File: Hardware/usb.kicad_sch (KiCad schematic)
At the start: 8 parts, among them J2 USB_C_Receptacle_USB2.0

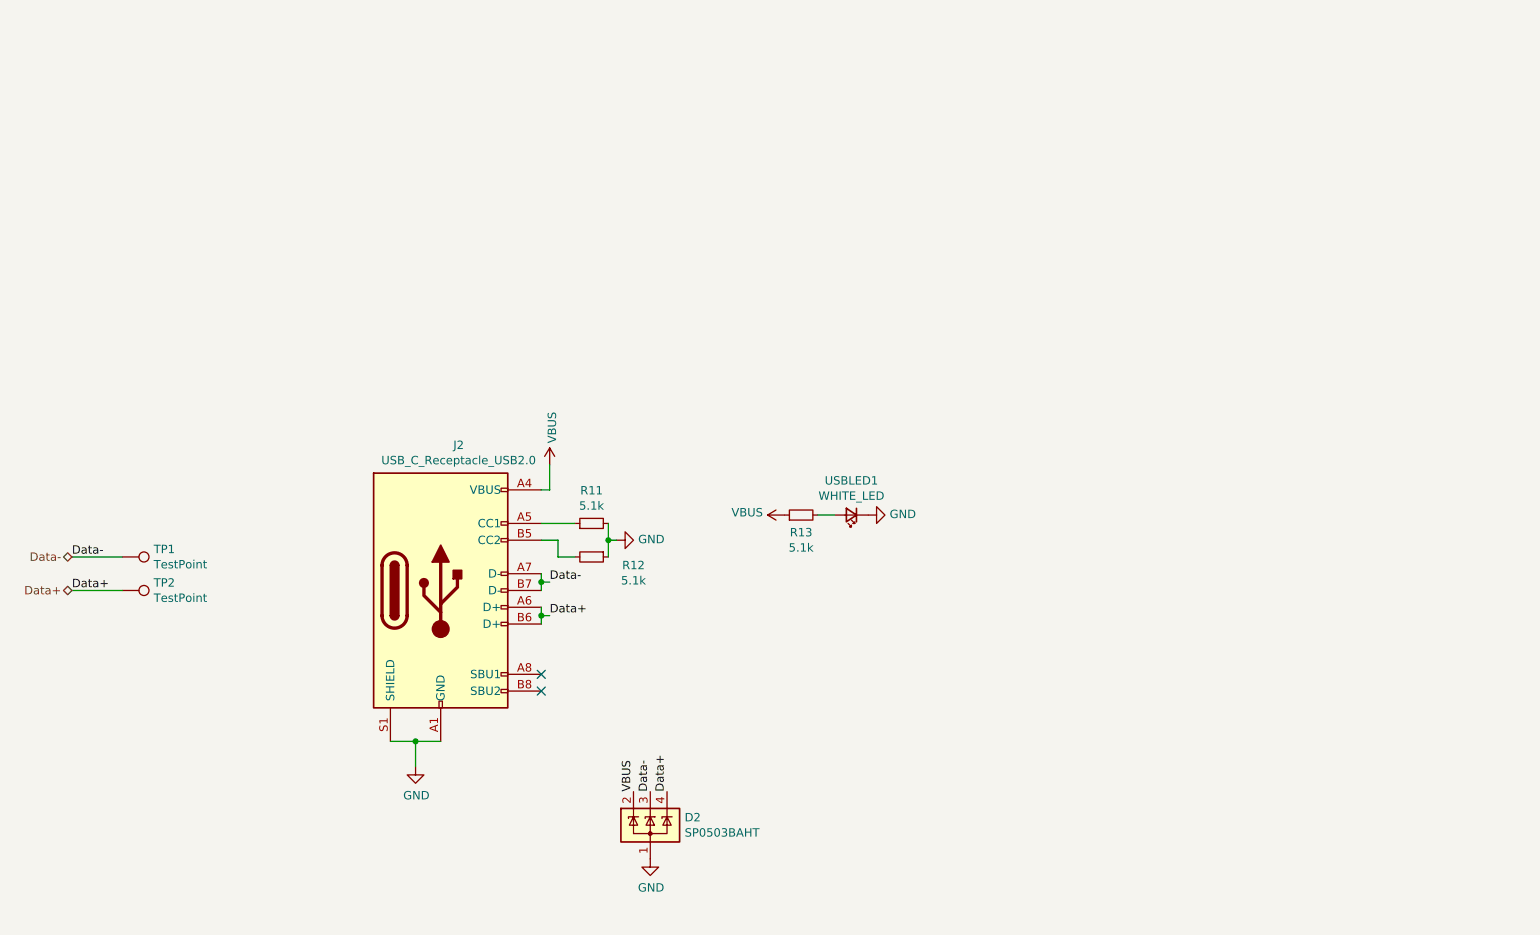
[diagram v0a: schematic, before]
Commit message: Revert "Merge remote-tracking branch 'refs/remotes/origin/main'"
This reverts commit c9a99cb72454eddb78504ad976151236a8d13e5c, reversing
changes made to 3cdb2e540a9938f01cf78ecb1078cc5742e66bb5.
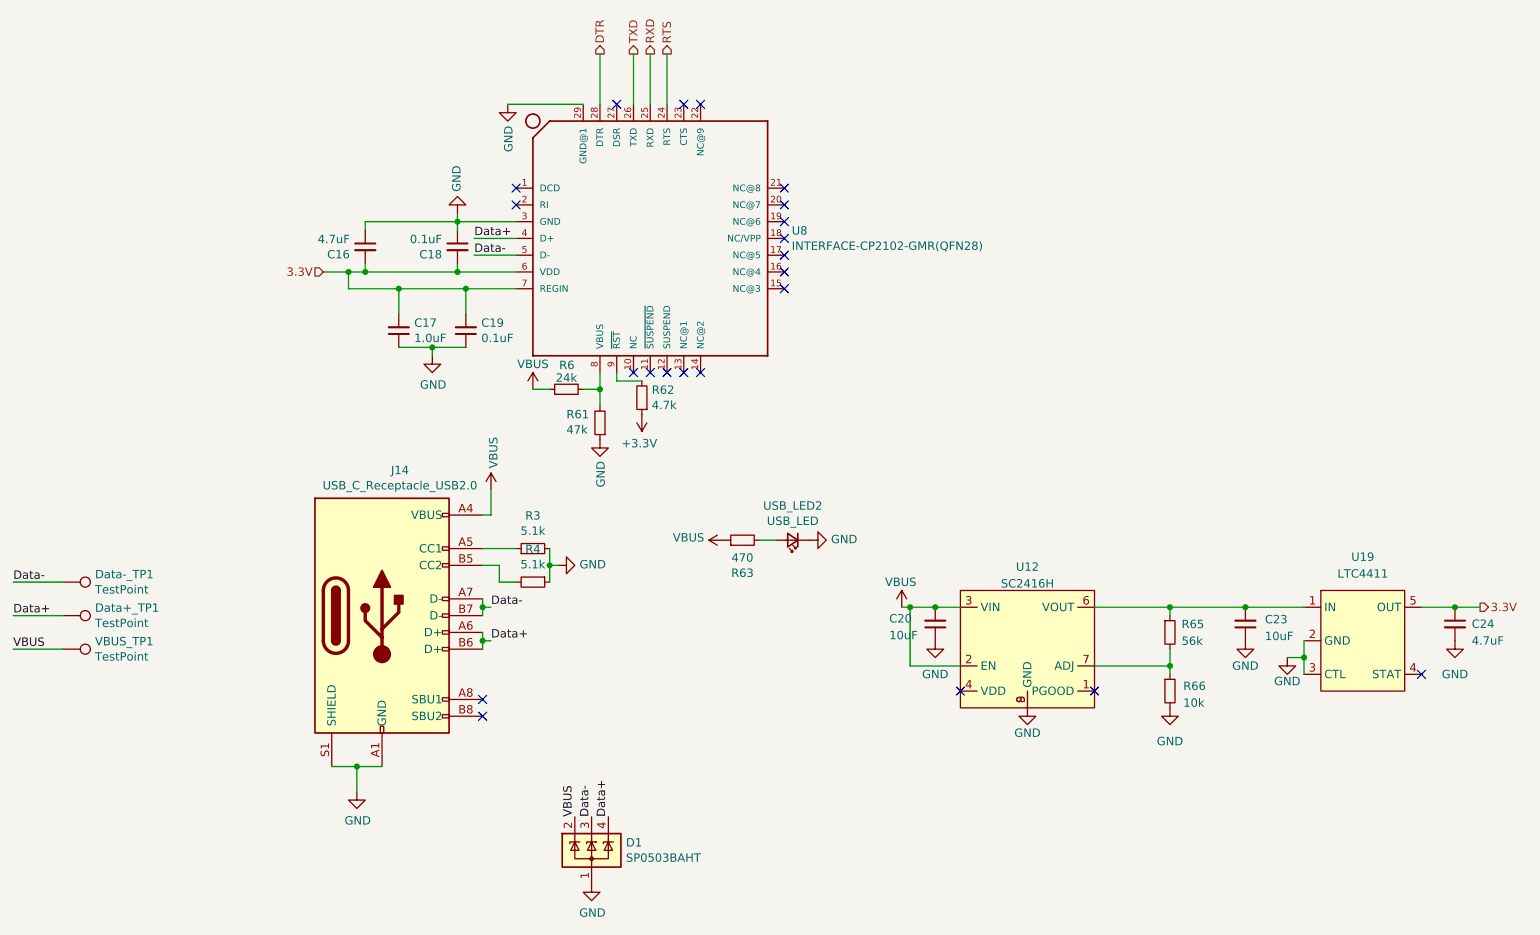
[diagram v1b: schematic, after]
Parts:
- removed D2: SP0503BAHT, Package_TO_SOT_SMD:SOT-143, symbol Power_Protection:SP0503BAHT
- removed J2: USB_C_Receptacle_USB2.0, Connector_USB:USB_C_Receptacle_Palconn_UTC16-G, symbol Connector:USB_C_Receptacle_USB2.0
- removed R11, R12, R13: 5.1k, Resistor_SMD:R_0402_1005Metric, symbol Device:R_Small
- removed TP1, TP2: TestPoint, TestPoint:TestPoint_Pad_D1.0mm, symbol Connector:TestPoint
- removed USBLED1: WHITE_LED, Resistor_SMD:R_0402_1005Metric, symbol Device:LED_Small
- added C16, C24: 4.7uF, Capacitor_SMD:C_0603_1608Metric, symbol Device:C_Small
- added C17: 1.0uF, Capacitor_SMD:C_0603_1608Metric, symbol Device:C_Small
- added C18, C19: 0.1uF, Capacitor_SMD:C_0603_1608Metric, symbol Device:C_Small
- added C20, C23: 10uF, Capacitor_SMD:C_0603_1608Metric, symbol Device:C_Small
- added D1: SP0503BAHT, Package_TO_SOT_SMD:SOT-143, symbol Power_Protection:SP0503BAHT
- added Data+_TP1, Data-_TP1, VBUS_TP1: TestPoint, TestPoint:TestPoint_Pad_D1.0mm, symbol Connector:TestPoint
- added J14: USB_C_Receptacle_USB2.0, Connector_USB:USB_C_Receptacle_GCT_USB4085, symbol Connector:USB_C_Receptacle_USB2.0
- added R3, R4: 5.1k, Resistor_SMD:R_0603_1608Metric, symbol Device:R_Small
- added R6: 24k, Resistor_SMD:R_0603_1608Metric, symbol Device:R_Small
- added R61: 47k, Resistor_SMD:R_0603_1608Metric, symbol Device:R_Small
- added R62: 4.7k, Resistor_SMD:R_0603_1608Metric, symbol Device:R_Small
- added R63: 470, Resistor_SMD:R_0603_1608Metric, symbol Device:R_Small
- added R65: 56k, Resistor_SMD:R_0603_1608Metric, symbol Device:R_Small
- added R66: 10k, Resistor_SMD:R_0603_1608Metric, symbol Device:R_Small
- added U12: SC2416H, iclr:SOIC127P599X175-9N, symbol iclr:RT9025-25GSP
- added U19: LTC4411, Package_TO_SOT_SMD:SOT-23-5, symbol iclr:LTC4411
- added U8: INTERFACE-CP2102-GMR(QFN28), iclr:QFN28G_0.5-5X5MM, symbol iclr:INTERFACE-CP2102-GMR(QFN28)
- added USB_LED2: USB_LED, LED_SMD:LED_0603_1608Metric, symbol Device:LED_Small
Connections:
- net Data+: now also D1.4 (K), Data+_TP1.1, J14.A6 (D+), J14.B6 (D+), U8.4 (D+)
- net Data-: now also D1.3 (K), Data-_TP1.1, J14.A7 (D-), J14.B7 (D-), U8.5 (D-)
- net GND: now also C16.1, C17.1, C18.1, C19.1, C20.1, C23.1, C24.2, D1.1 (A), J14.A1 (GND), J14.A12 (GND), J14.B1 (GND), J14.B12 (GND), J14.S1 (SHIELD), R3.2, R4.1, R61.1, R66.2, U12.8 (GND), U12.9 (GND), U19.2 (GND), U19.3 (CTL), U8.29 (GND@1), U8.3 (GND), USB_LED2.1 (K)
- net VBUS: now also C20.2, D1.2 (K), J14.A4 (VBUS), J14.A9 (VBUS), J14.B4 (VBUS), J14.B9 (VBUS), R6.1, R63.1, U12.2 (EN), U12.3 (VIN), VBUS_TP1.1
- new net: J14.A5 (CC1), R3.1
- new net: C23.2, R65.1, U12.6 (VOUT), U19.1 (IN)
- new net: R63.2, USB_LED2.2 (A)
- new net: R65.2, R66.1, U12.7 (ADJ)
- new net: R6.2, R61.2, U8.8 (VBUS)
- new net: J14.B5 (CC2), R4.2
- new net: R62.2, U8.9 (~{RST})
- new net +3V3: R62.1
- new net 3.3V: C16.2, C17.2, C18.2, C19.2, C24.1, U19.5 (OUT), U8.6 (VDD), U8.7 (REGIN)
- new net DTR: U8.28 (DTR)
- new net RTS: U8.24 (RTS)
- new net RXD: U8.25 (RXD)
- new net TXD: U8.26 (TXD)
- no-connect marks 2 -> 22

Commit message: Start of Kermit Mini
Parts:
- removed C16, C24: 4.7uF, Capacitor_SMD:C_0603_1608Metric, symbol Device:C_Small
- removed C17: 1.0uF, Capacitor_SMD:C_0603_1608Metric, symbol Device:C_Small
- removed C18, C19: 0.1uF, Capacitor_SMD:C_0603_1608Metric, symbol Device:C_Small
- removed C20, C23: 10uF, Capacitor_SMD:C_0603_1608Metric, symbol Device:C_Small
- removed D1: SP0503BAHT, Package_TO_SOT_SMD:SOT-143, symbol Power_Protection:SP0503BAHT
- removed Data+_TP1, Data-_TP1, VBUS_TP1: TestPoint, TestPoint:TestPoint_Pad_D1.0mm, symbol Connector:TestPoint
- removed J14: USB_C_Receptacle_USB2.0, Connector_USB:USB_C_Receptacle_GCT_USB4085, symbol Connector:USB_C_Receptacle_USB2.0
- removed R3, R4: 5.1k, Resistor_SMD:R_0603_1608Metric, symbol Device:R_Small
- removed R6: 24k, Resistor_SMD:R_0603_1608Metric, symbol Device:R_Small
- removed R61: 47k, Resistor_SMD:R_0603_1608Metric, symbol Device:R_Small
- removed R62: 4.7k, Resistor_SMD:R_0603_1608Metric, symbol Device:R_Small
- removed R63: 470, Resistor_SMD:R_0603_1608Metric, symbol Device:R_Small
- removed R65: 56k, Resistor_SMD:R_0603_1608Metric, symbol Device:R_Small
- removed R66: 10k, Resistor_SMD:R_0603_1608Metric, symbol Device:R_Small
- removed U12: SC2416H, iclr:SOIC127P599X175-9N, symbol iclr:RT9025-25GSP
- removed U19: LTC4411, Package_TO_SOT_SMD:SOT-23-5, symbol iclr:LTC4411
- removed U8: INTERFACE-CP2102-GMR(QFN28), iclr:QFN28G_0.5-5X5MM, symbol iclr:INTERFACE-CP2102-GMR(QFN28)
- removed USB_LED2: USB_LED, LED_SMD:LED_0603_1608Metric, symbol Device:LED_Small
- added D2: SP0503BAHT, Package_TO_SOT_SMD:SOT-143, symbol Power_Protection:SP0503BAHT
- added J2: USB_C_Receptacle_USB2.0, Connector_USB:USB_C_Receptacle_Palconn_UTC16-G, symbol Connector:USB_C_Receptacle_USB2.0
- added R11, R12, R13: 5.1k, Resistor_SMD:R_0402_1005Metric, symbol Device:R_Small
- added TP1, TP2: TestPoint, TestPoint:TestPoint_Pad_D1.0mm, symbol Connector:TestPoint
- added USBLED1: WHITE_LED, Resistor_SMD:R_0402_1005Metric, symbol Device:LED_Small
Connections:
- net Data+: now also D2.4 (K), J2.A6 (D+), J2.B6 (D+), TP2.1
- net Data-: now also D2.3 (K), J2.A7 (D-), J2.B7 (D-), TP1.1
- net GND: now also D2.1 (A), J2.A1 (GND), J2.A12 (GND), J2.B1 (GND), J2.B12 (GND), J2.S1 (SHIELD), R11.2, R12.1, USBLED1.1 (K)
- net VBUS: now also D2.2 (K), J2.A4 (VBUS), J2.A9 (VBUS), J2.B4 (VBUS), J2.B9 (VBUS), R13.1
- new net: J2.B5 (CC2), R12.2
- new net: J2.A5 (CC1), R11.1
- new net: R13.2, USBLED1.2 (A)
- no-connect marks 22 -> 2
